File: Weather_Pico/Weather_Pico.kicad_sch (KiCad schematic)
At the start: 19 parts, among them J1 Pwr In, J2 12V, J3 Rain 3 Adv, J4 WIND, J5 RAIN 1, J6 Rain 2 Serial, J7 Debug, SW1 RUN, U1 Pico, U2 L7805

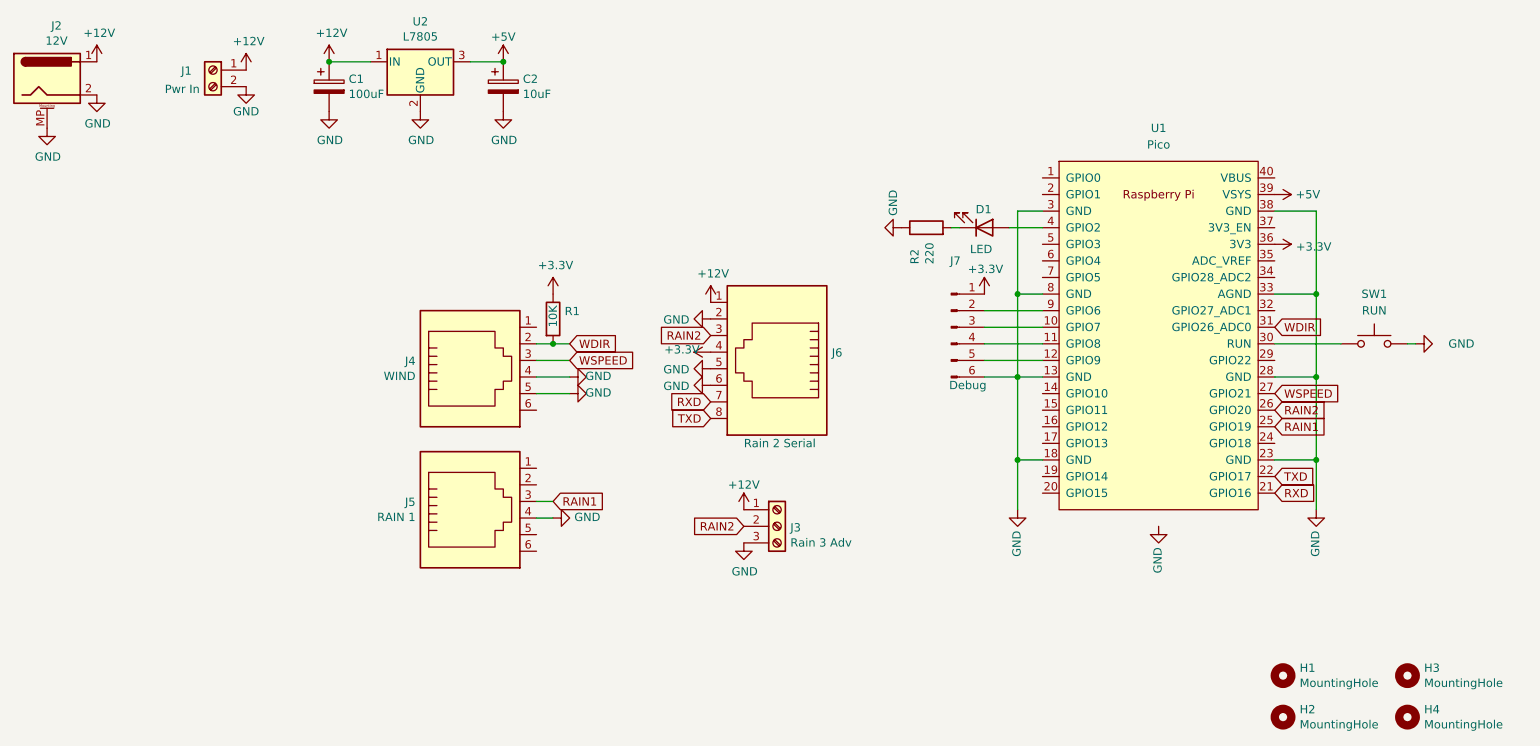
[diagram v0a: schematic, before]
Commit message: added temperature headers
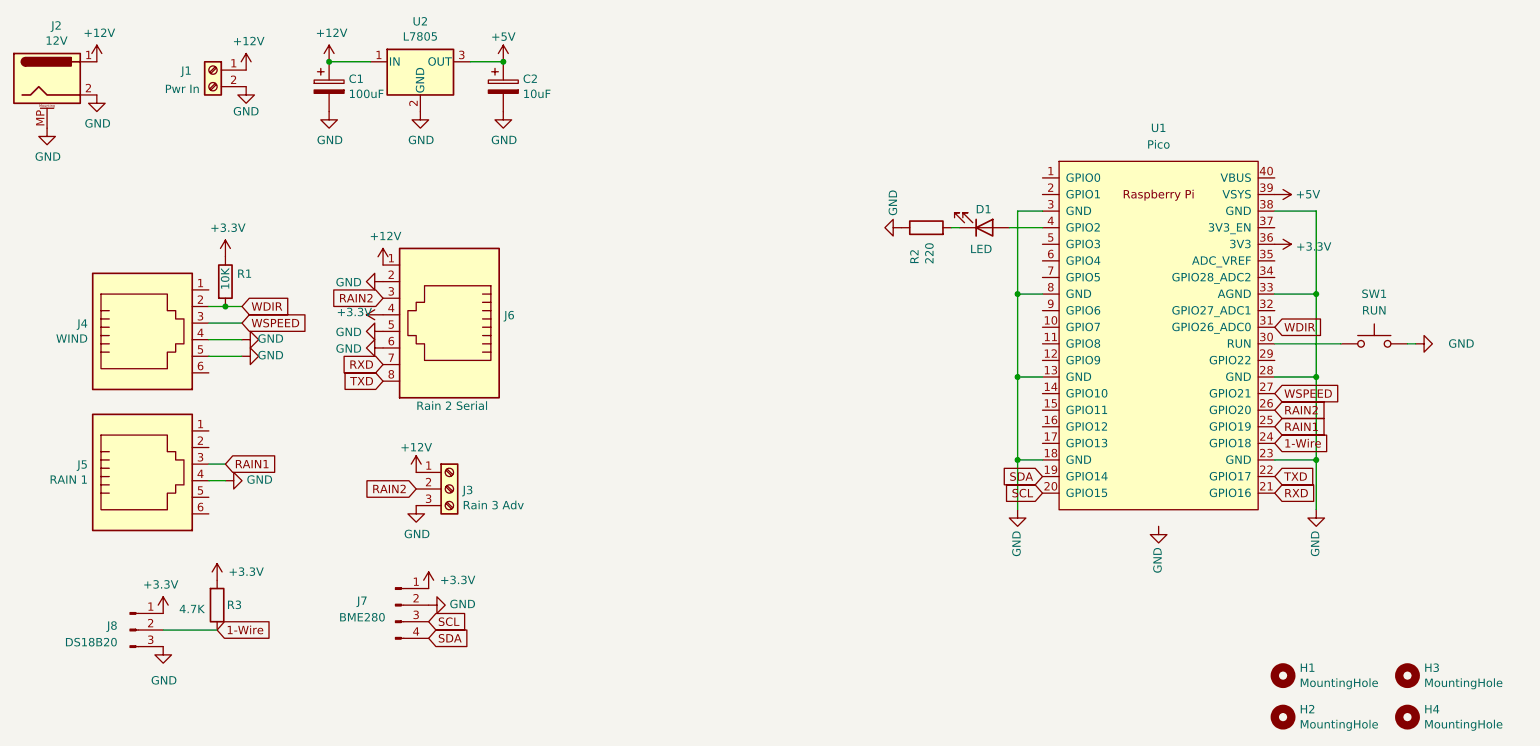
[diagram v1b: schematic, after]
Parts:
- removed J7: Debug, Weather_Pico:1x06_Horizontal_SMD, symbol Connector:Conn_01x06_Male
- added J7: BME280, Connector_PinHeader_2.54mm:PinHeader_1x04_P2.54mm_Vertical, symbol Connector:Conn_01x04_Pin
- added J8: DS18B20, Connector_JST:JST_XH_B3B-XH-A_1x03_P2.50mm_Vertical, symbol Connector:Conn_01x03_Pin
- added R3: 4.7K, Resistor_THT:R_Axial_DIN0207_L6.3mm_D2.5mm_P7.62mm_Horizontal, symbol Device:R
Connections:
- net +3V3: now also J7.1 (Pin_1), J8.1 (Pin_1), R3.2
- net GND: now also J7.2 (Pin_2), J8.3 (Pin_3)
- net SDA: now reaches U1.19 (GPIO14)
- net SDA: now also J7.4 (Pin_4)
- net SCL: now reaches U1.20 (GPIO15)
- net SCL: now also J7.3 (Pin_3)
- net 1-Wire: now reaches U1.24 (GPIO18)
- net 1-Wire: now also J8.2 (Pin_2), R3.1
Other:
- moved on the sheet: J3, J4, J5, J6, R1
